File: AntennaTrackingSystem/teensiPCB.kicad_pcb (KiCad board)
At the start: 2 copper layers, 45 x 84 mm, 12 parts, among them J1 screw terminal, J5 UART1, J6 UART2, J7 I2C ext, SW1 SW_Push, U1 Teensy4.1, U2 SAM-M10Q-00B

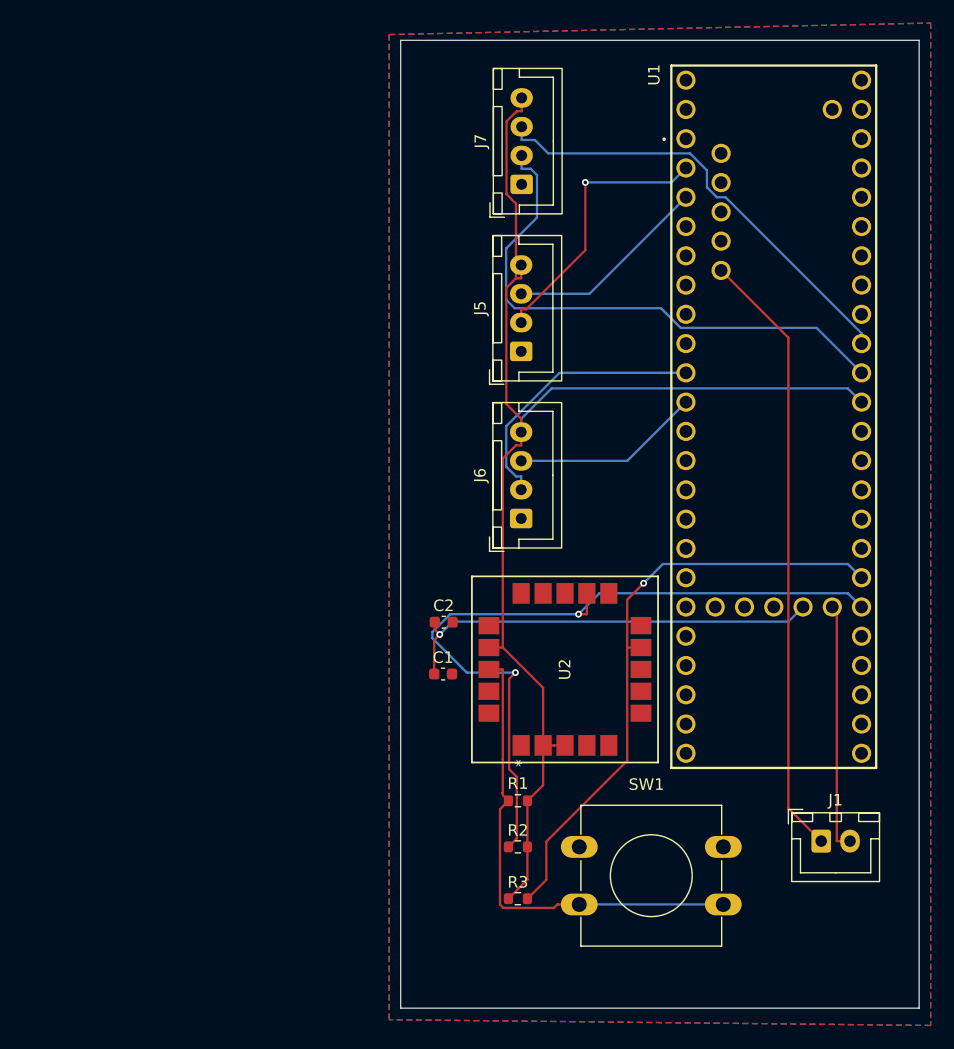
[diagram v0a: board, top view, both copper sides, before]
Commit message: ground plane chanegs
changed ground plane
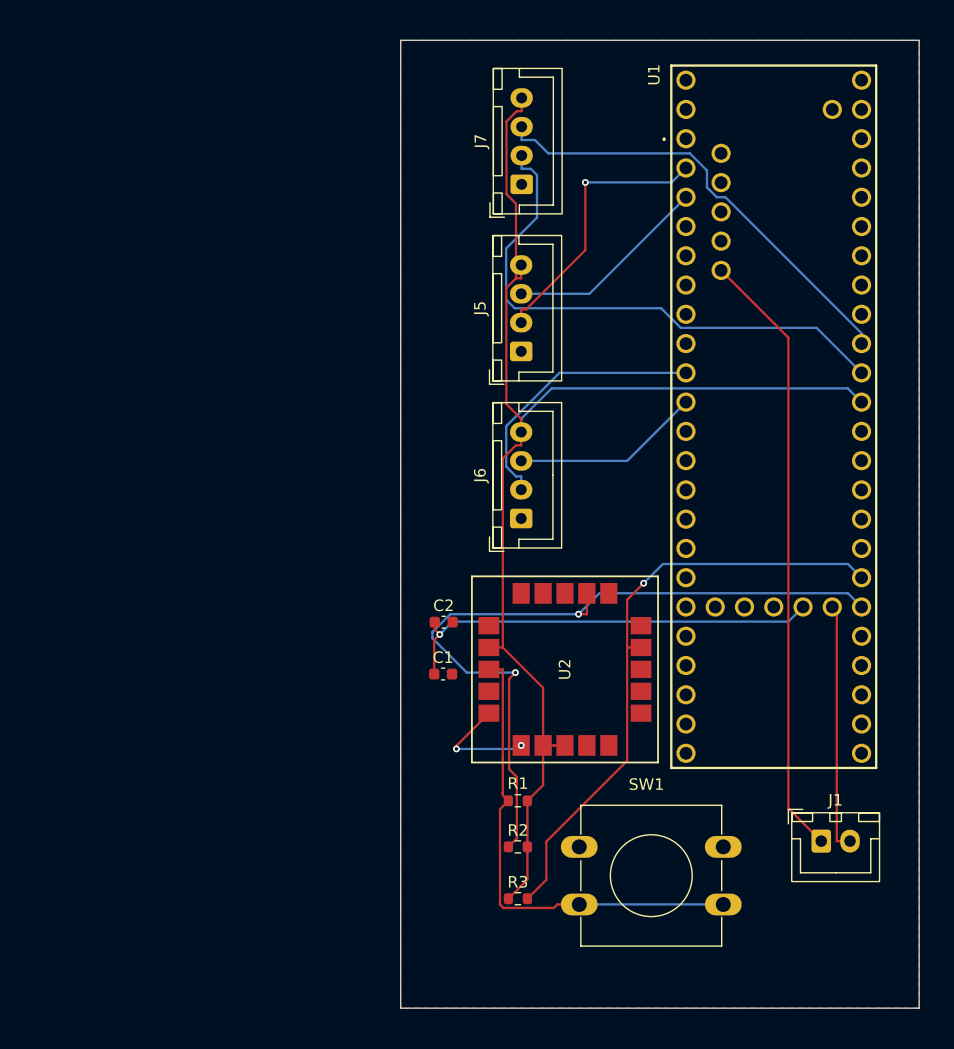
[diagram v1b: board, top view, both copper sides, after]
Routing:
- net GND: track 0.00 -> 10.0 mm, vias 0 -> 2
- removed copper zone on B.Cu, net GND
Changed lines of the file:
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@@
 			(layer "F.Fab")
 		)
-		(fp_text user "*"
-			(at -8.136701 -3.8 90)
-			(layer "F.SilkS")
-			(effects
-				(font
-					(size 1 1)
-					(thickness 0.15)
-				)
-			)
-		)
-		(fp_text user "*"
-			(at -8.136701 -3.8 90)
-			(unlocked yes)
-			(layer "F.SilkS")
-			(effects
-				(font
-					(size 1 1)
-					(thickness 0.15)
-				)
-			)
-		)
-		(fp_text user "*"
-			(at -5.063301 -3.8 90)
-			(unlocked yes)
-			(layer "F.Fab")
-			(effects
-				(font
-					(size 1 1)
-					(thickness 0.15)
-				)
-			)
-		)
 		(fp_text user "${REFERENCE}"
 			(at 0 0 90)
@@
 	)
 	(segment
+		(start 177.34 120.219998)
+		(end 177.34 120.5)
+		(width 0.2)
+		(layer "F.Cu")
+		(net 1)
+	)
+	(segment
+		(start 180.159998 117.4)
+		(end 177.34 120.219998)
+		(width 0.2)
+		(layer "F.Cu")
+		(net 1)
+	)
+	(via
+		(at 177.34 120.5)
+		(size 0.6)
+		(drill 0.3)
+		(layers "F.Cu" "B.Cu")
+		(net 1)
+	)
+	(via
+		(at 182.96 120.200002)
+		(size 0.6)
+		(drill 0.3)
+		(layers "F.Cu" "B.Cu")
+		(net 1)
+	)
+	(segment
+		(start 177.34 120.5)
+		(end 182.660002 120.5)
+		(width 0.2)
+		(layer "B.Cu")
+		(net 1)
+	)
+	(segment
+		(start 182.660002 120.5)
+		(end 182.96 120.200002)
+		(width 0.2)
+		(layer "B.Cu")
+		(net 1)
+	)
+	(segment
 		(start 175.41 114)
 		(end 175.41 111.0492)
@@
 		(net 1)
 		(net_name "GND")
-		(layers "F.Cu" "B.Cu")
+		(layer "F.Cu")
 		(hatch edge 0.5)
 		(connect_pads
@@
 		(min_thickness 0.25)
 		(filled_areas_thickness no)
-		(fill
+		(fill yes
 			(thermal_gap 0.5)
 			(thermal_bridge_width 0.5)
@@
 		(polygon
 			(pts
-				(xy 171.5 58.5) (xy 218.5 57.5) (xy 218.5 144.5) (xy 171.5 144)
+				(xy 172.51 59.01) (xy 217.5 59.01) (xy 217.5 143) (xy 172.5 143)
 			)
 		)

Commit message: changes
added battery chnages
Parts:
- added J2: Conn_01x02, Connector_JST:JST_XH_B2B-XH-A_1x02_P2.50mm_Vertical, F.Cu at (208.9, 137.0)
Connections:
- J1 pad 1: /+V -> Net-(J1-Pin_1)
- J1 pad 2: Net-(J1-Pin_2) -> GND
- U1 pad 47: Net-(J1-Pin_2) -> GND
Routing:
- net /+V: track 53.1 -> 114.7 mm
- net Net-(J1-Pin_2): track 21.6 -> 0.00 mm
- net GND: track 10.0 -> 31.6 mm
- net Net-(J1-Pin_1): track 0.00 -> 9.04 mm

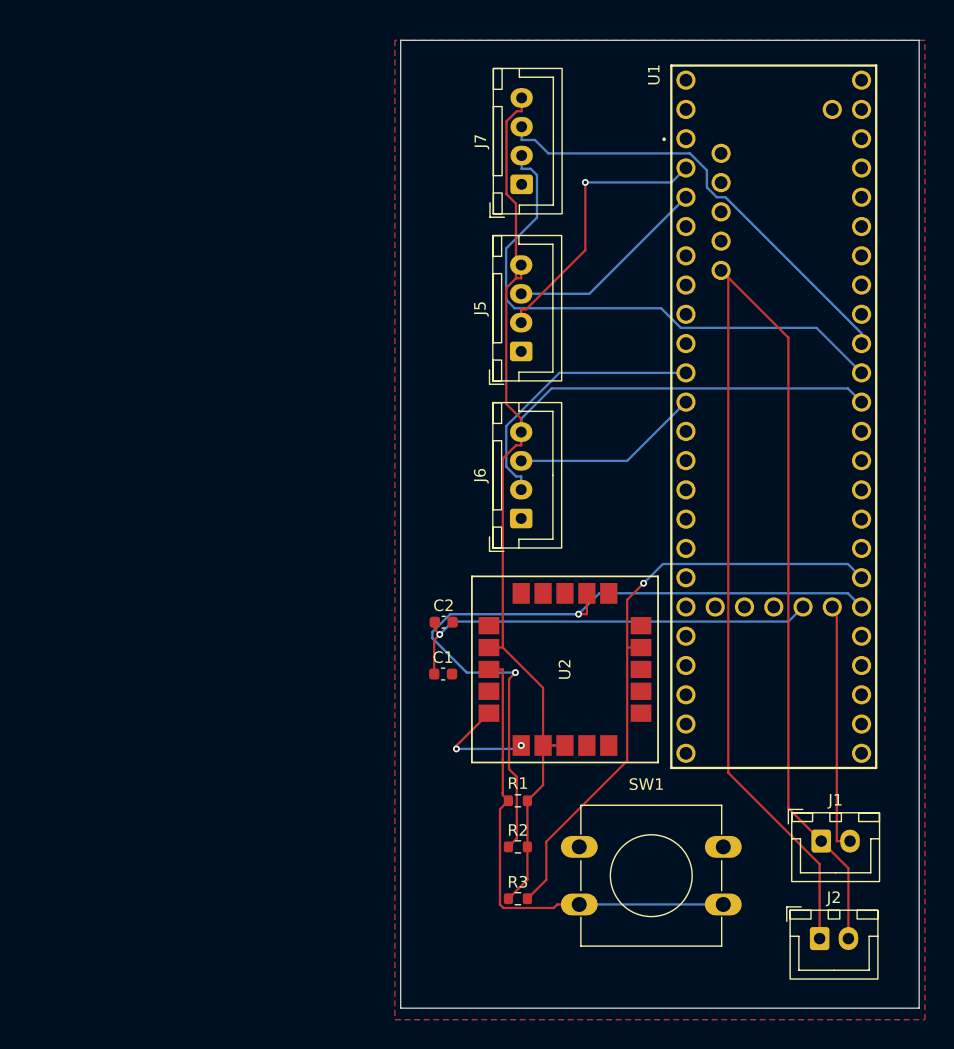
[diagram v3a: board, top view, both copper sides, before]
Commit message: Footprint corrections
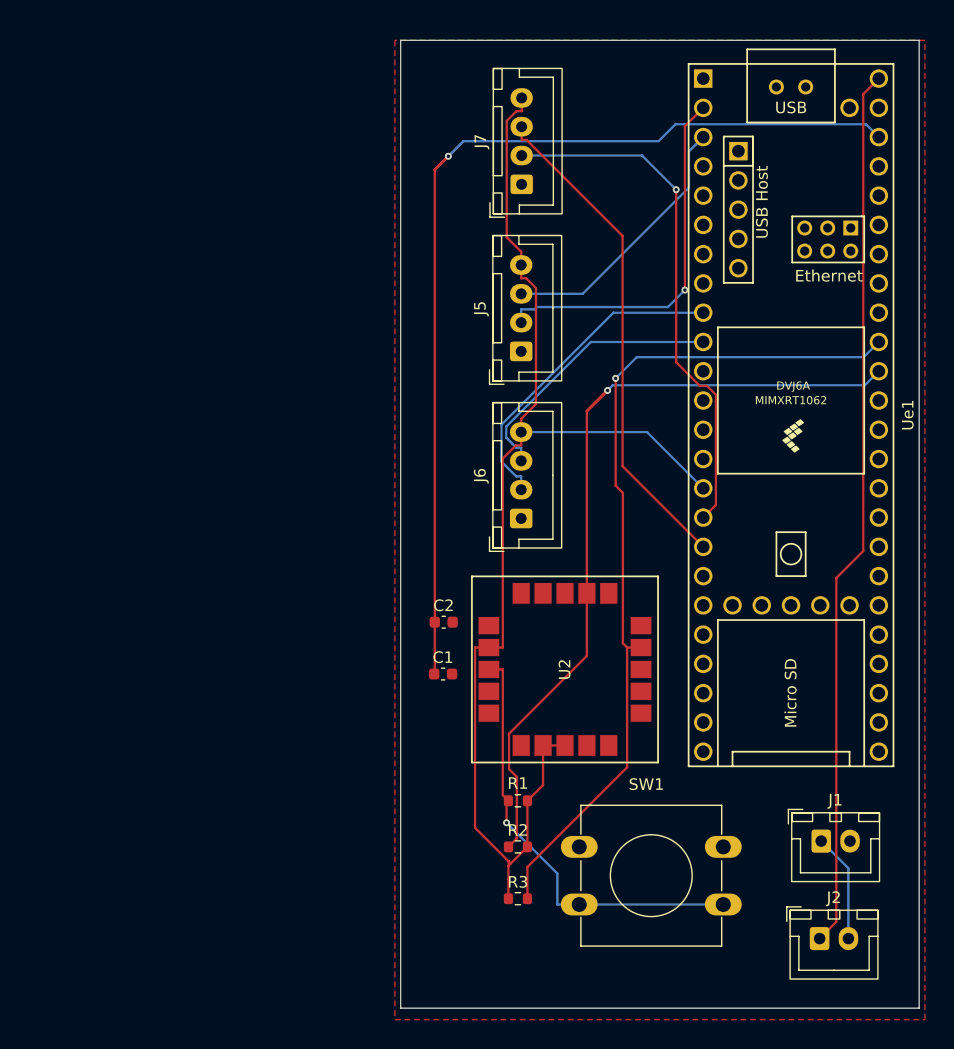
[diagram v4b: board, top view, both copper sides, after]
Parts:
- Ue1: renamed from U1; footprint Teensy41:TEENSY41 -> avionicsKiCadLibrary:Teensy41
- moved Ue1 25.7 mm to (206.4, 91.5)
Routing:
- net Net-(C1-Pad1): track 37.4 -> 91.1 mm
- net /+V: track 114.7 -> 76.8 mm
- net GND: track 31.6 -> 0.00 mm, vias 2 -> 0
- net Net-(U2-SDA): track 52.9 -> 74.5 mm
- net Net-(U2-SCL): track 66.6 -> 78.1 mm, vias 2 -> 1
- net Net-(J5-Pin_2): track 24.0 -> 32.5 mm
- net Net-(J6-Pin_3): track 16.4 -> 23.9 mm
- net Net-(J5-Pin_3): track 17.8 -> 23.3 mm
- net Net-(J6-Pin_2): track 23.8 -> 28.1 mm
- net Net-(J7-Pin_3): track 39.4 -> 43.2 mm
- net +3V3: track 112.1 -> 108.3 mm
- net Net-(U2-RESET_N): track 41.7 -> 38.1 mm, vias 0 -> 1
- net Net-(J7-Pin_2): track 48.1 -> 45.3 mm, vias 0 -> 1

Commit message: teensy footprint
forgot to save
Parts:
- added H1: MountingHole, MountingHole:MountingHole_3.2mm_M3, F.Cu at (141.3, 77.5)
- added H2: MountingHole, MountingHole:MountingHole_3.2mm_M3, F.Cu at (141.3, 85.4)
- U2: footprint SAM M10Q footprint:SAM-M10Q_UBL -> SAM-M10Q:SAM-M10Q_UBL
- Ue1: footprint avionicsKiCadLibrary:Teensy41 -> teensy:teensy
- turned Ue1 to 0 degrees
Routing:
- net +3V3: track 108.3 -> 0.00 mm
- net Net-(C1-Pad1): track 91.1 -> 0.00 mm, vias 1 -> 0
- net Net-(U2-SCL): track 78.1 -> 0.00 mm, vias 1 -> 0
- net /+V: track 76.8 -> 0.00 mm
- net Net-(U2-SDA): track 74.5 -> 0.00 mm, vias 1 -> 0
- net Net-(J7-Pin_2): track 45.3 -> 0.00 mm, vias 1 -> 0
- net Net-(J7-Pin_3): track 43.2 -> 0.00 mm
- net Net-(U2-RESET_N): track 38.1 -> 0.00 mm, vias 1 -> 0
- net Net-(J5-Pin_2): track 32.5 -> 0.00 mm, vias 1 -> 0
- net Net-(J6-Pin_2): track 28.1 -> 0.00 mm
- net Net-(J6-Pin_3): track 23.9 -> 0.00 mm
- net Net-(J5-Pin_3): track 23.3 -> 0.00 mm
- net Net-(J1-Pin_1): track 9.44 -> 0.00 mm

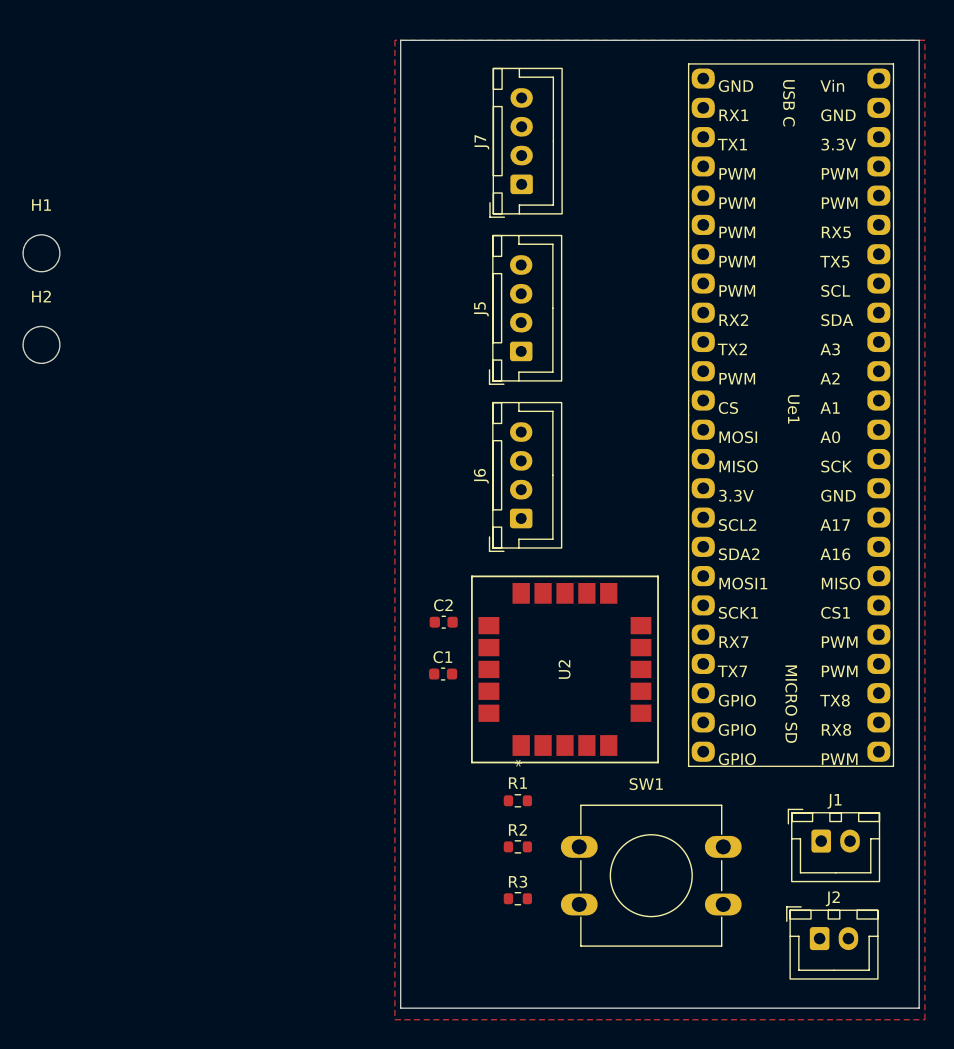
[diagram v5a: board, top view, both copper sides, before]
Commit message: updated footprint
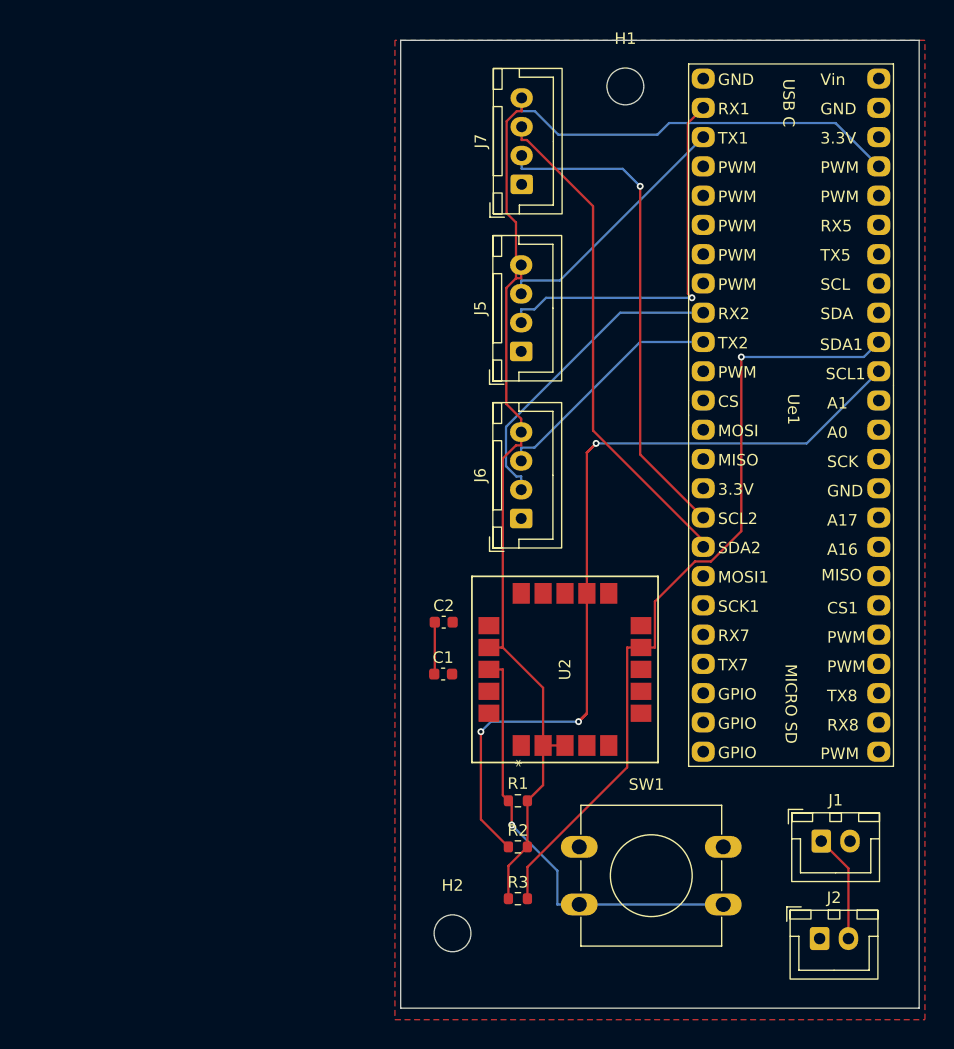
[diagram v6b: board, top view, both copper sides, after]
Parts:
- moved H2 62.3 mm to (177.0, 136.5)
- moved H1 52.7 mm to (192.0, 63.0)
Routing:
- net +3V3: track 0.00 -> 114.8 mm
- net Net-(U2-SCL): track 0.00 -> 80.4 mm, vias 0 -> 3
- net Net-(U2-SDA): track 0.00 -> 69.4 mm, vias 0 -> 1
- net Net-(J7-Pin_3): track 0.00 -> 43.3 mm
- net Net-(J7-Pin_2): track 0.00 -> 43.1 mm, vias 0 -> 1
- net Net-(U2-RESET_N): track 0.00 -> 38.0 mm, vias 0 -> 1
- net Net-(J5-Pin_2): track 0.00 -> 33.6 mm, vias 0 -> 1
- net Net-(J6-Pin_2): track 0.00 -> 27.5 mm
- net Net-(J5-Pin_3): track 0.00 -> 22.1 mm
- net Net-(J6-Pin_3): track 0.00 -> 20.7 mm
- net Net-(J1-Pin_1): track 0.00 -> 9.44 mm
- net Net-(C1-Pad1): track 0.00 -> 4.52 mm
